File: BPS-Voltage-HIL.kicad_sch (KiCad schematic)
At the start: 3 parts, among them J3 SOMConnector, U2 DAC7311xDCK, U4 DAC7311xDCK

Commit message: push
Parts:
- added C1, C2, C6, C7: 10u, Capacitor_SMD:C_0805_2012Metric_Pad1.18x1.45mm_HandSolder, symbol Device:C_Small
- added C3, C4, C5, C8: 0.1u, Capacitor_SMD:C_0805_2012Metric_Pad1.18x1.45mm_HandSolder, symbol Device:C_Small
- added J1: Conn_01x02_Socket, Connector_Molex:Molex_Micro-Fit_3.0_43045-0212_2x01_P3.00mm_Vertical, symbol Connector:Conn_01x02_Socket
- added J2: Out1_1, Connector_Molex:Molex_Micro-Fit_3.0_43650-0815_1x08_P3.00mm_Vertical, symbol Connector:Conn_01x08_Socket
- added J4: Out1_2, Connector_Molex:Molex_Micro-Fit_3.0_43650-0815_1x08_P3.00mm_Vertical, symbol Connector:Conn_01x08_Socket
- added J5: Out2_1, Connector_Molex:Molex_Micro-Fit_3.0_43650-0815_1x08_P3.00mm_Vertical, symbol Connector:Conn_01x08_Socket
- added J6: Out2_2, Connector_Molex:Molex_Micro-Fit_3.0_43650-0815_1x08_P3.00mm_Vertical, symbol Connector:Conn_01x08_Socket
- added U1, U3: DAC7311xDCK, Package_TO_SOT_SMD:SOT-363_SC-70-6, symbol Analog_DAC:DAC7311xDCK
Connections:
- net +5V: now also C1.1, C2.1, C3.2, C4.2, C5.2, C6.1, C7.1, C8.2, J1.1 (Pin_1), U1.4 (AVDD/AVREF), U3.4 (AVDD/AVREF)
- net GND: now also C1.2, C2.2, C3.1, C4.1, C5.1, C6.2, C7.2, C8.1, J1.2 (Pin_2), U1.5 (GND), U3.5 (GND)
- net SPI1_MOSI: now also U4.3 (DIN)
- net SPI1_SCK: now also U4.2 (SCLK)
- net SPI2_MOSI: now also U1.3 (DIN), U3.3 (DIN); no longer U4.3 (DIN)
- net SPI2_SCK: now also U1.2 (SCLK), U3.2 (SCLK); no longer U4.2 (SCLK)
- net DAC1_OUT renamed jumpers/DAC1_OUT
- net DAC2_OUT renamed jumpers/DAC2_OUT
- net I2C2_SCL renamed CS3
- net CS3: now also U1.1 (~{SYNC})
- net I2C2_SDA renamed CS4
- net CS4: now also U3.1 (~{SYNC})
- net PA1 renamed CS1
- net CS1: now also U2.1 (~{SYNC})
- net PA2 renamed CS2
- net CS2: now also U4.1 (~{SYNC})
- net SPI1_NSS: no longer names the net of J3.19
- net SPI1_NSS: no longer U2.1 (~{SYNC})
- net SPI2_NSS: no longer names the net of J3.7
- net SPI2_NSS: no longer U4.1 (~{SYNC})
- new net Out1_1_1: J2.1 (Pin_1)
- new net Out1_1_2: J2.2 (Pin_2)
- new net Out1_1_3: J2.3 (Pin_3)
- new net Out1_1_4: J2.4 (Pin_4)
- new net Out1_1_5: J2.5 (Pin_5)
- new net Out1_1_6: J2.6 (Pin_6)
- new net Out1_1_7: J2.7 (Pin_7)
- new net Out1_1_8: J2.8 (Pin_8)
- new net Out1_2_1: J4.1 (Pin_1)
- new net Out1_2_2: J4.2 (Pin_2)
- new net Out1_2_3: J4.3 (Pin_3)
- new net Out1_2_4: J4.4 (Pin_4)
- new net Out1_2_5: J4.5 (Pin_5)
- new net Out1_2_6: J4.6 (Pin_6)
- new net Out1_2_7: J4.7 (Pin_7)
- new net Out1_2_8: J4.8 (Pin_8)
- new net Out2_1_1: J5.1 (Pin_1)
- new net Out2_1_2: J5.2 (Pin_2)
- new net Out2_1_3: J5.3 (Pin_3)
- new net Out2_1_4: J5.4 (Pin_4)
- new net Out2_1_5: J5.5 (Pin_5)
- new net Out2_1_6: J5.6 (Pin_6)
- new net Out2_1_7: J5.7 (Pin_7)
- new net Out2_1_8: J5.8 (Pin_8)
- new net Out2_2_1: J6.1 (Pin_1)
- new net Out2_2_2: J6.2 (Pin_2)
- new net Out2_2_3: J6.3 (Pin_3)
- new net Out2_2_4: J6.4 (Pin_4)
- new net Out2_2_5: J6.5 (Pin_5)
- new net Out2_2_6: J6.6 (Pin_6)
- new net Out2_2_7: J6.7 (Pin_7)
- new net Out2_2_8: J6.8 (Pin_8)
- new net jumpers/DAC3_OUT: U1.6 (VOUT)
- new net jumpers/DAC4_OUT: U3.6 (VOUT)
- no-connect marks 0 -> 2
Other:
- added sheet jumpers (jumpers.kicad_sch)
- moved on the sheet: U2, U4

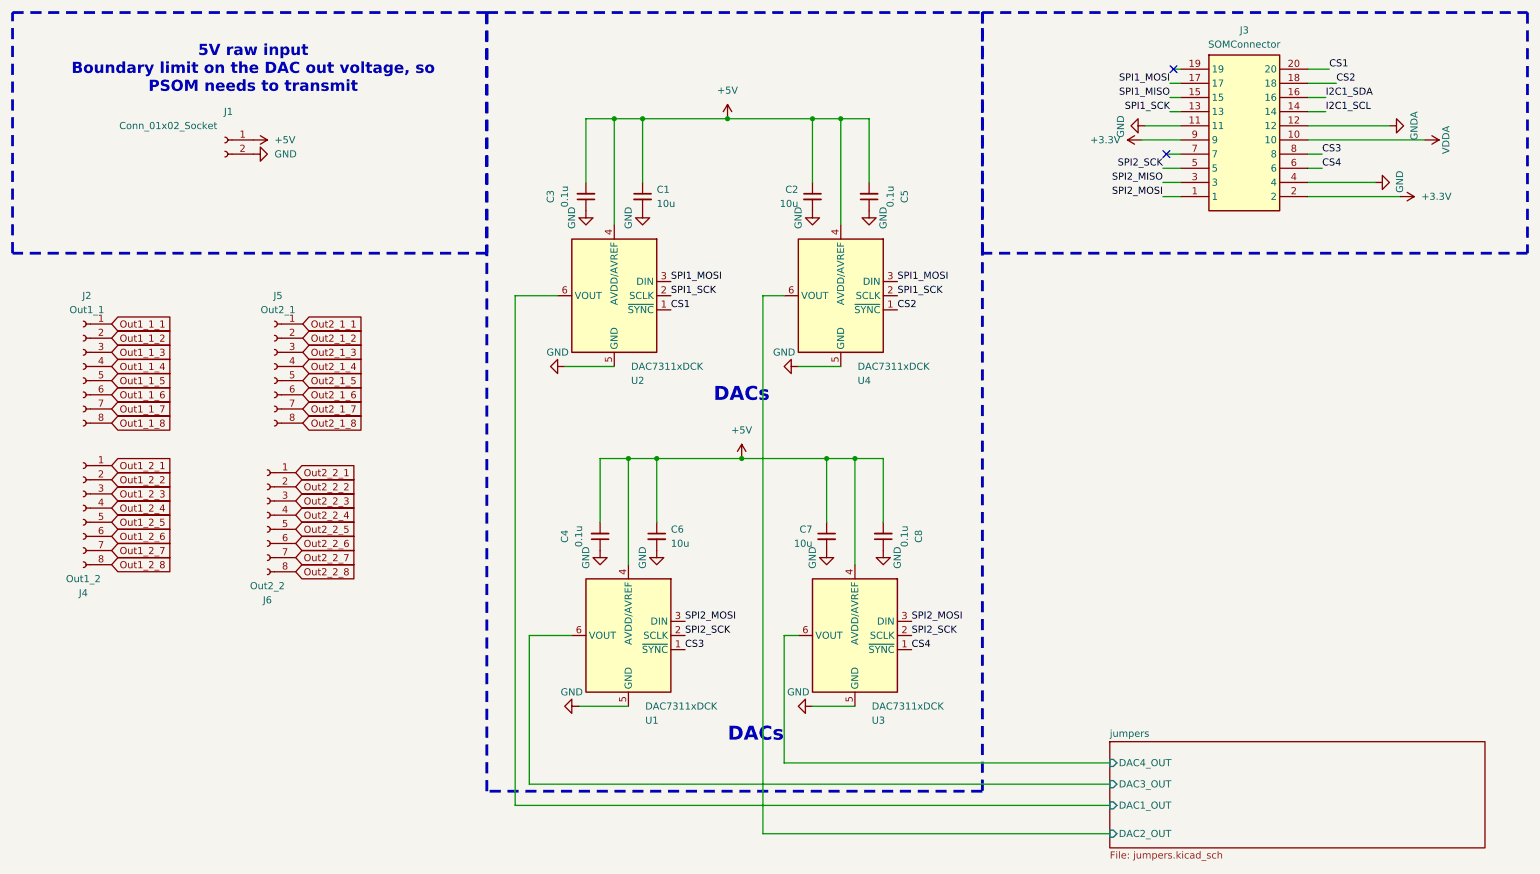
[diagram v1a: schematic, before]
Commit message: psom connector footprint is not right
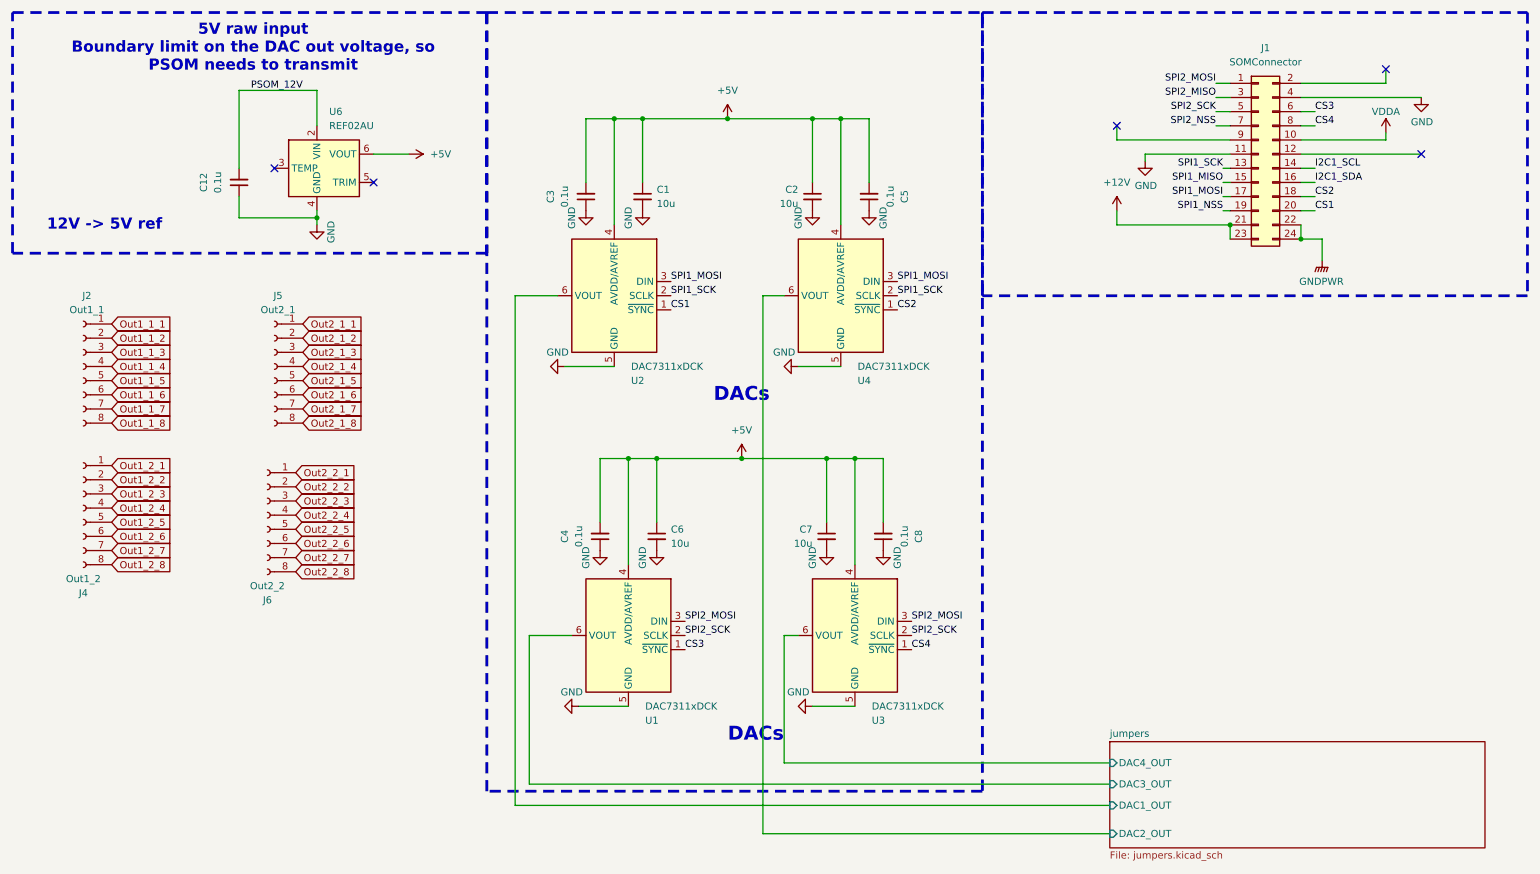
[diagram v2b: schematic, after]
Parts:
- removed J1: Conn_01x02_Socket, Connector_Molex:Molex_Micro-Fit_3.0_43045-0212_2x01_P3.00mm_Vertical, symbol Connector:Conn_01x02_Socket
- removed J3: SOMConnector, UTSVT_Connectors:Molex_52465-2070, symbol utsvt-connectors:SOMConnector
- added C12: 0.1u, Capacitor_SMD:C_0805_2012Metric_Pad1.18x1.45mm_HandSolder, symbol Device:C_Small
- added J1: SOMConnector, UTSVT_Connectors:Molex_53307-2071, symbol Connector_Generic:Conn_02x12_Odd_Even
- added U6: REF02AU, Package_SO:SOIC-8_3.9x4.9mm_P1.27mm, symbol Reference_Voltage:REF02AU
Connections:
- net +5V: now also U6.6 (VOUT)
- net CS1: now also J1.20 (Pin_20)
- net CS2: now also J1.18 (Pin_18)
- net CS3: now also J1.6 (Pin_6)
- net CS4: now also J1.8 (Pin_8)
- net GND: now also C12.1, J1.11 (Pin_11), J1.4 (Pin_4), U6.4 (GND)
- net I2C1_SCL: now also J1.14 (Pin_14)
- net I2C1_SDA: now also J1.16 (Pin_16)
- net SPI1_MISO: now also J1.15 (Pin_15)
- net SPI1_MOSI: now also J1.17 (Pin_17)
- net SPI1_SCK: now also J1.13 (Pin_13)
- net SPI2_MISO: now also J1.3 (Pin_3)
- net SPI2_MOSI: now also J1.1 (Pin_1)
- net SPI2_SCK: now also J1.5 (Pin_5)
- net VDDA: now also J1.10 (Pin_10)
- new net +12V: J1.21 (Pin_21), J1.23 (Pin_23)
- new net GNDPWR: J1.22 (Pin_22), J1.24 (Pin_24)
- new net PSOM_12V: C12.2, U6.2 (VIN)
- new net SPI1_NSS: J1.19 (Pin_19)
- new net SPI2_NSS: J1.7 (Pin_7)
- no-connect marks 2 -> 5
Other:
- note added: "12V -> 5V ref"

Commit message: 12v input connectors, figure out can thingy
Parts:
- removed J1: SOMConnector, UTSVT_Connectors:Molex_53307-2071, symbol Connector_Generic:Conn_02x12_Odd_Even
- added J1: 52465-2470, UTSVT_Connectors:Molex_53307-2071, symbol utsvt-connectors:52465-2470
- added J3: 12V_IN, symbol Connector:Conn_01x02_Socket
- added J39: can_rx, symbol Connector:Conn_01x02_Socket
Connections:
- net CS1: now also J1.20
- net CS2: now also J1.18
- net CS3: now also J1.8
- net CS4: now also J1.6
- net GND: now also J1.11, J1.4; no longer C1.2, C12.1, C2.2, C3.1, C4.1, C5.1, C6.2, C7.2, C8.1, U1.5 (GND), U2.5 (GND), U3.5 (GND), U4.5 (GND), U6.4 (GND)
- net GNDPWR: now also C1.2, C12.1, C2.2, C3.1, C4.1, C5.1, C6.2, C7.2, C8.1, U1.5 (GND), U2.5 (GND), U3.5 (GND), U4.5 (GND), U6.4 (GND), J1.24, J3.1 (Pin_1)
- net I2C1_SCL: now also J1.14
- net I2C1_SDA: now also J1.16
- net SPI1_MISO: now also J1.15
- net SPI1_MOSI: now also J1.17
- net SPI1_NSS: now also J1.19
- net SPI1_SCK: now also J1.13
- net SPI2_MISO: now also J1.3
- net SPI2_MOSI: now also J1.1
- net SPI2_NSS: now also J1.7
- net SPI2_SCK: now also J1.5
- net VDDA: now also J1.10
- net PSOM_12V: no longer names the net of C12.2, U6.2 (VIN)
- net PSOM_12V: now also J3.2 (Pin_2)
- new net +3.3V: J1.2, J1.9
- new net 12V_Ext: J1.22
- new net CAN_H: J1.23
- new net CAN_L: J1.21
- new net GNDA: J1.12
- no-connect marks 5 -> 3
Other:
- note added: "PSOM Mezzanine receiver"
- note removed: "5V raw input Boundary limit on the DAC out voltage, so PSOM needs to transmit"
